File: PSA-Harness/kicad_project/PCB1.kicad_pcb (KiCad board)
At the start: 4 copper layers, 22.4 x 43.8 mm, 5 parts, among them J10 B2B_1, J11 B2B_2, J4 to_car_1, J5 to_car_2, J6 to_car_3

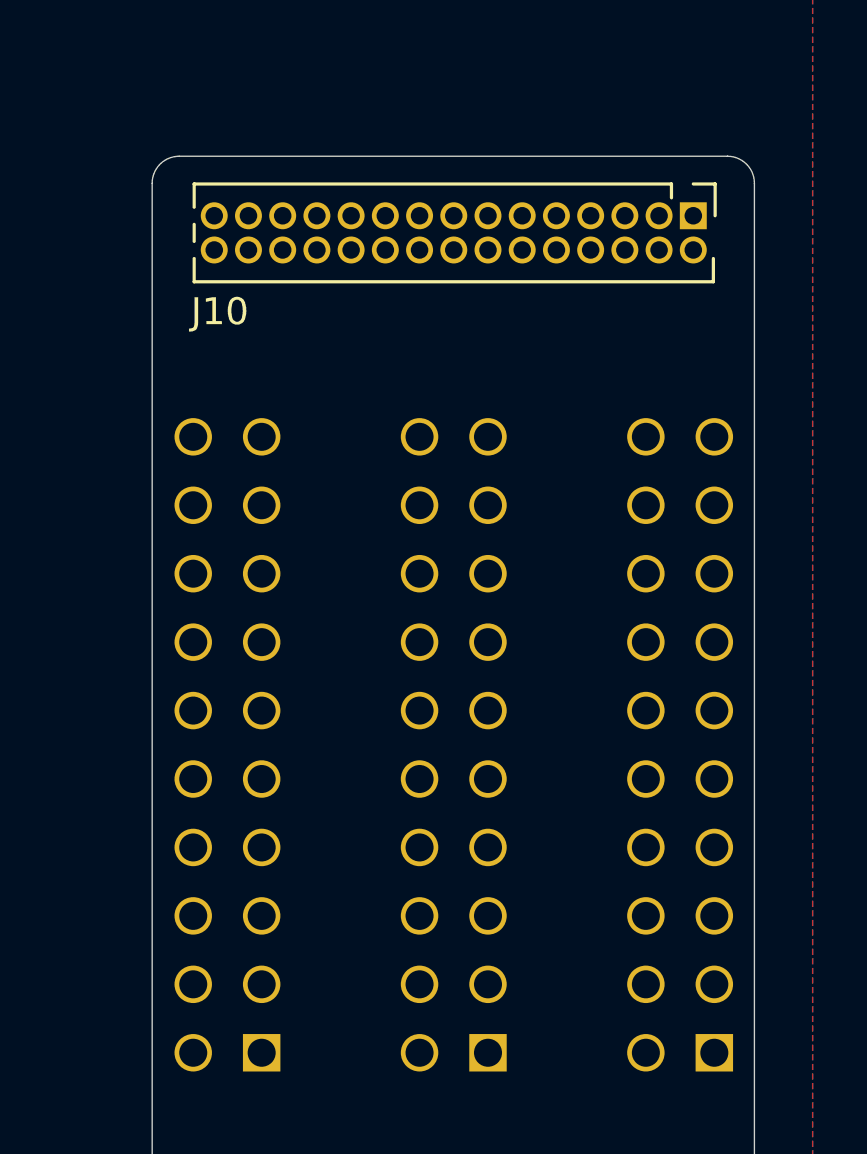
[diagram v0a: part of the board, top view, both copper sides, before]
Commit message: CAN routing PCB1
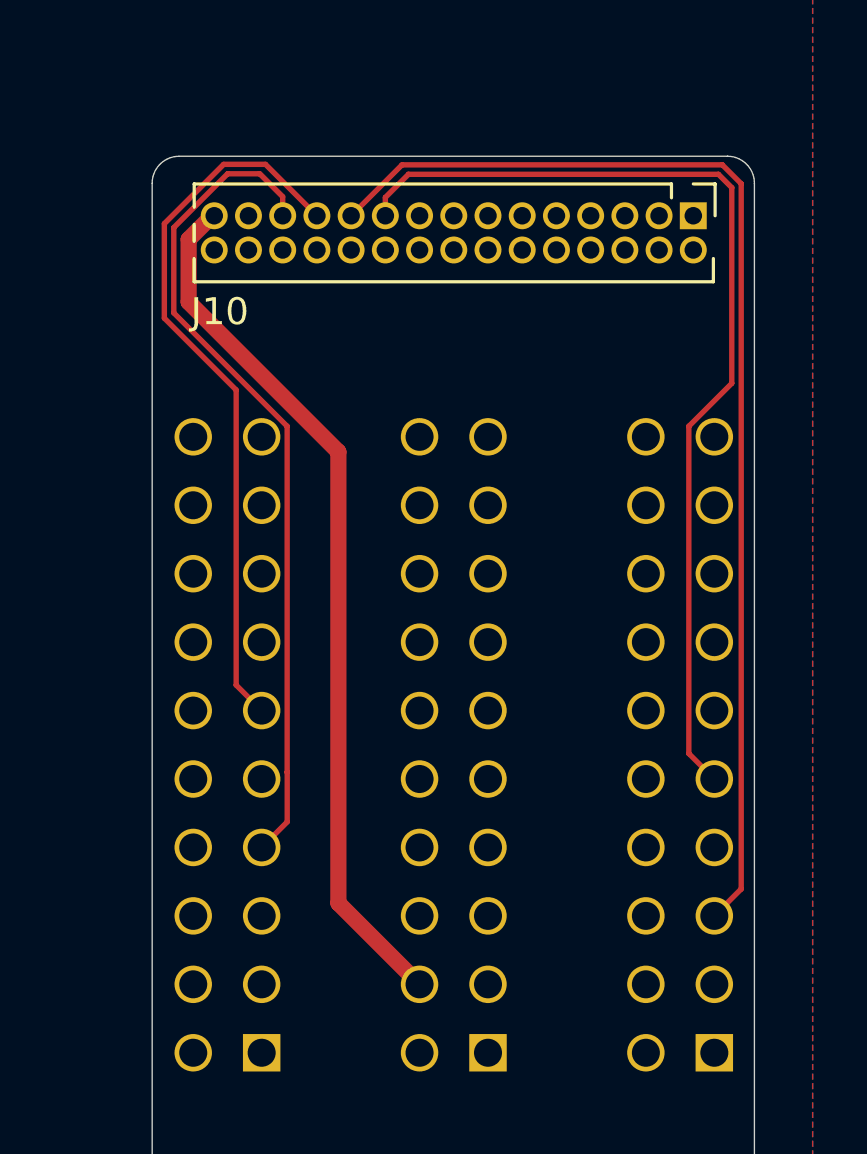
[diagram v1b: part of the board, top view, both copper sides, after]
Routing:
- net CAN2_L: track 0.00 -> 43.1 mm
- net CAN2_H: track 0.00 -> 37.1 mm
- net +12V: track 0.00 -> 32.5 mm
- net CAN1_L: track 0.00 -> 31.1 mm
- net CAN1_H: track 0.00 -> 26.9 mm

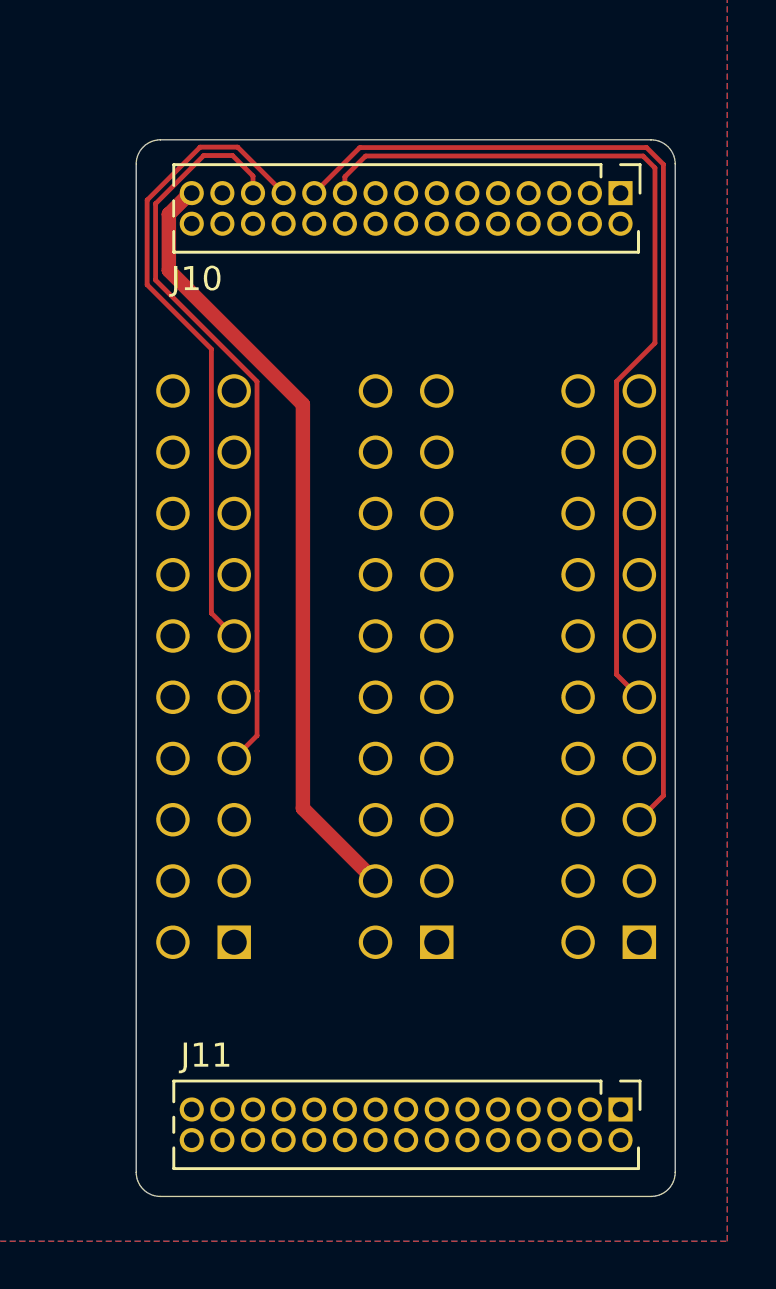
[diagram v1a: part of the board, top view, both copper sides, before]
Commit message: PCB1 routed
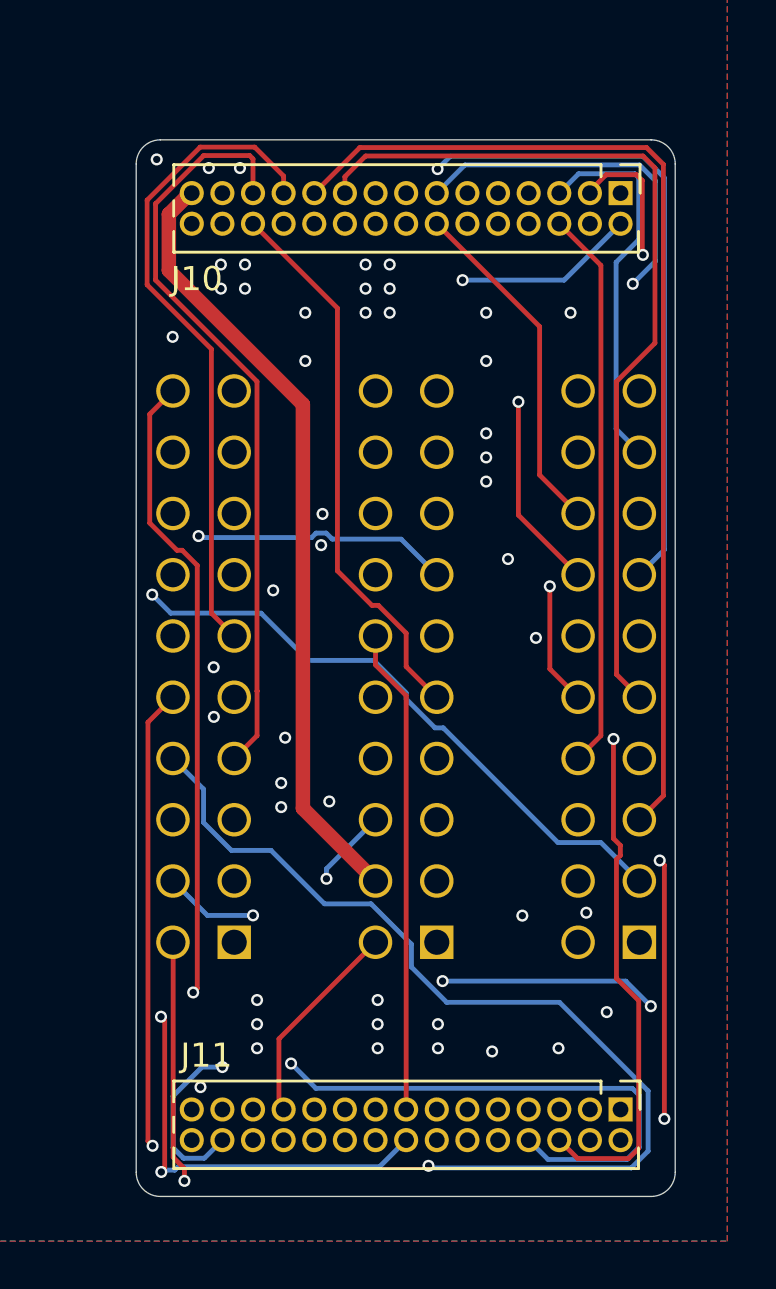
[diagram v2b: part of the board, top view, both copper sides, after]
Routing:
- net 1: track 0.00 -> 57.0 mm, vias 0 -> 2
- net 2: track 0.00 -> 54.8 mm, vias 0 -> 2
- net 50: track 0.00 -> 52.6 mm, vias 0 -> 3
- net 49: track 0.00 -> 48.6 mm, vias 0 -> 1
- net 48: track 0.00 -> 44.0 mm, vias 0 -> 1
- net 52: track 0.00 -> 42.1 mm, vias 0 -> 3
- net 54: track 0.00 -> 41.4 mm, vias 0 -> 1
- net 47: track 0.00 -> 41.1 mm, vias 0 -> 1
- net 28: track 0.00 -> 36.7 mm, vias 0 -> 1
- net 4: track 0.00 -> 34.9 mm, vias 0 -> 1
- net 30: track 0.00 -> 34.7 mm, vias 0 -> 1
- net 59: track 0.00 -> 34.5 mm, vias 0 -> 2
- net 12: track 0.00 -> 34.4 mm, vias 0 -> 1
- net 11: track 0.00 -> 33.4 mm
- net 29: track 0.00 -> 33.2 mm, vias 0 -> 1
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
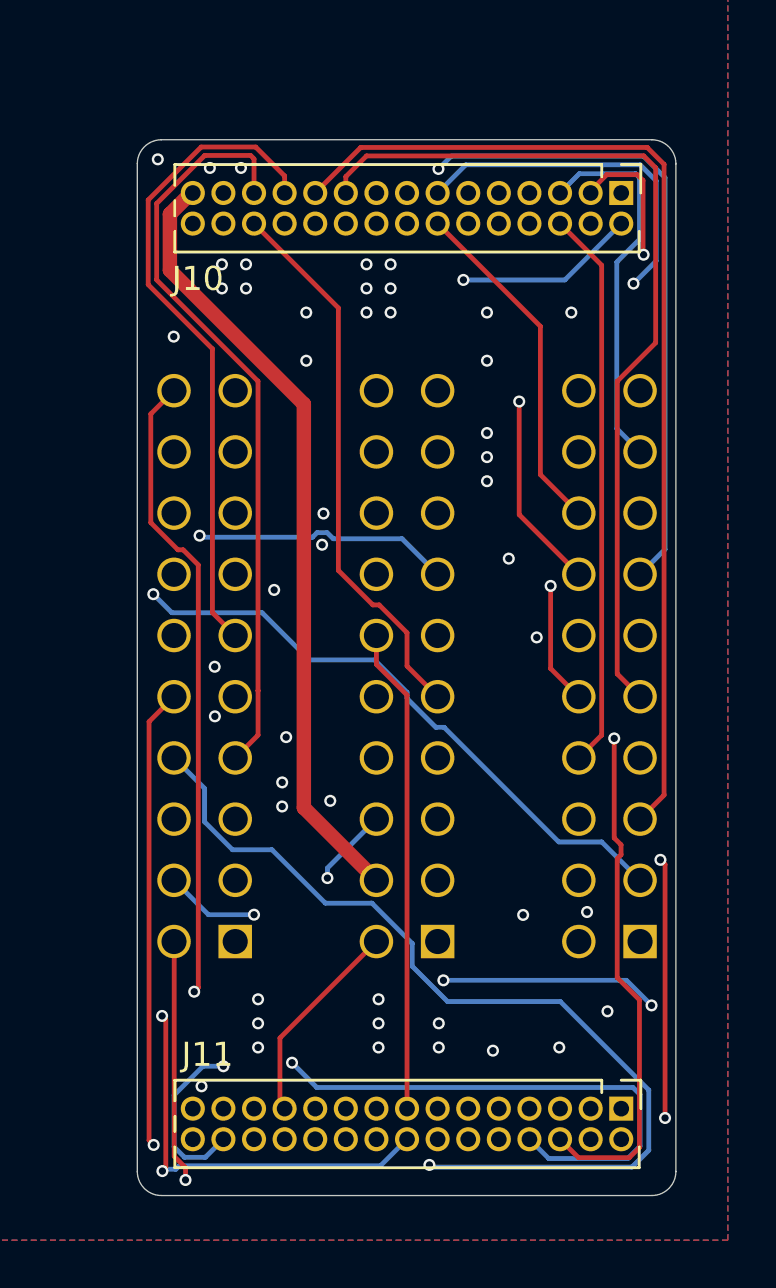
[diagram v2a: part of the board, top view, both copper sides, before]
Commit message: improve PCB1 clearences
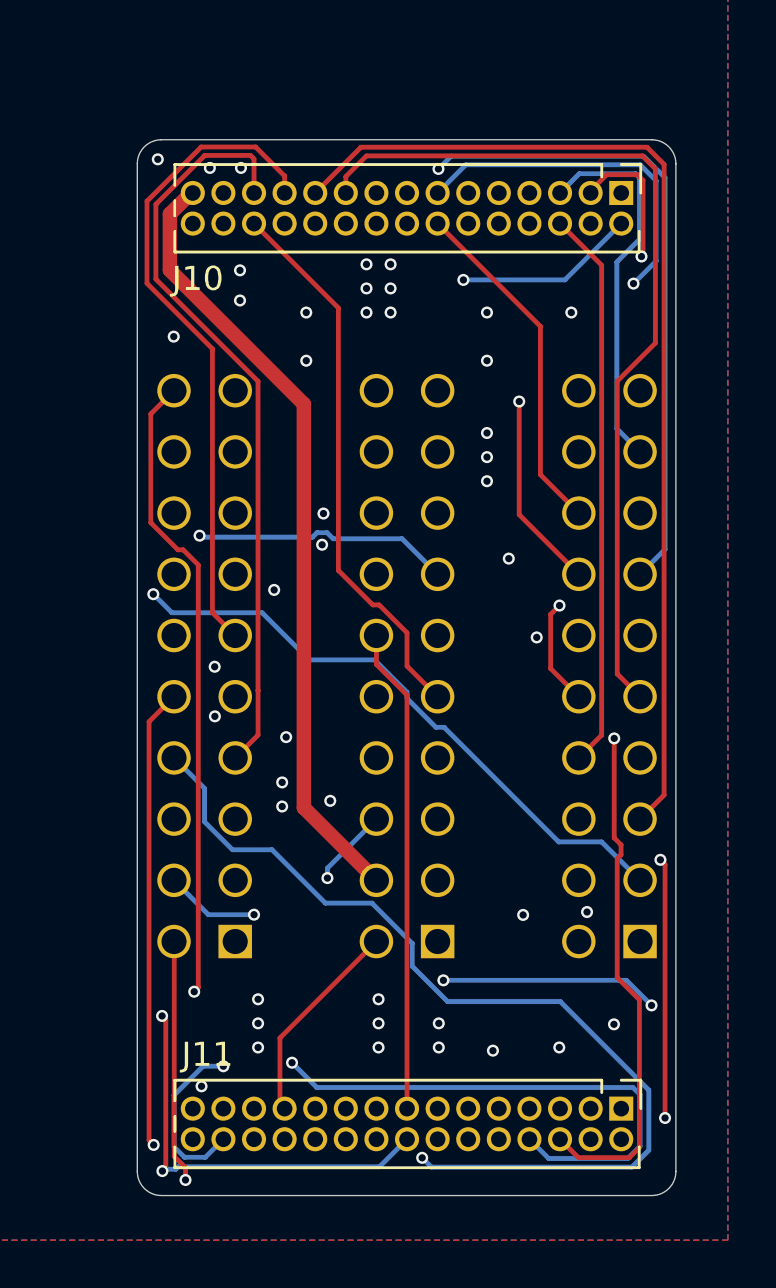
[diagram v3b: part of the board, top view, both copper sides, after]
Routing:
- net 16: track 18.5 -> 19.0 mm
- net GND: vias 34 -> 32
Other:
- rule pad_to_mask_clearance: 0.038 -> 0

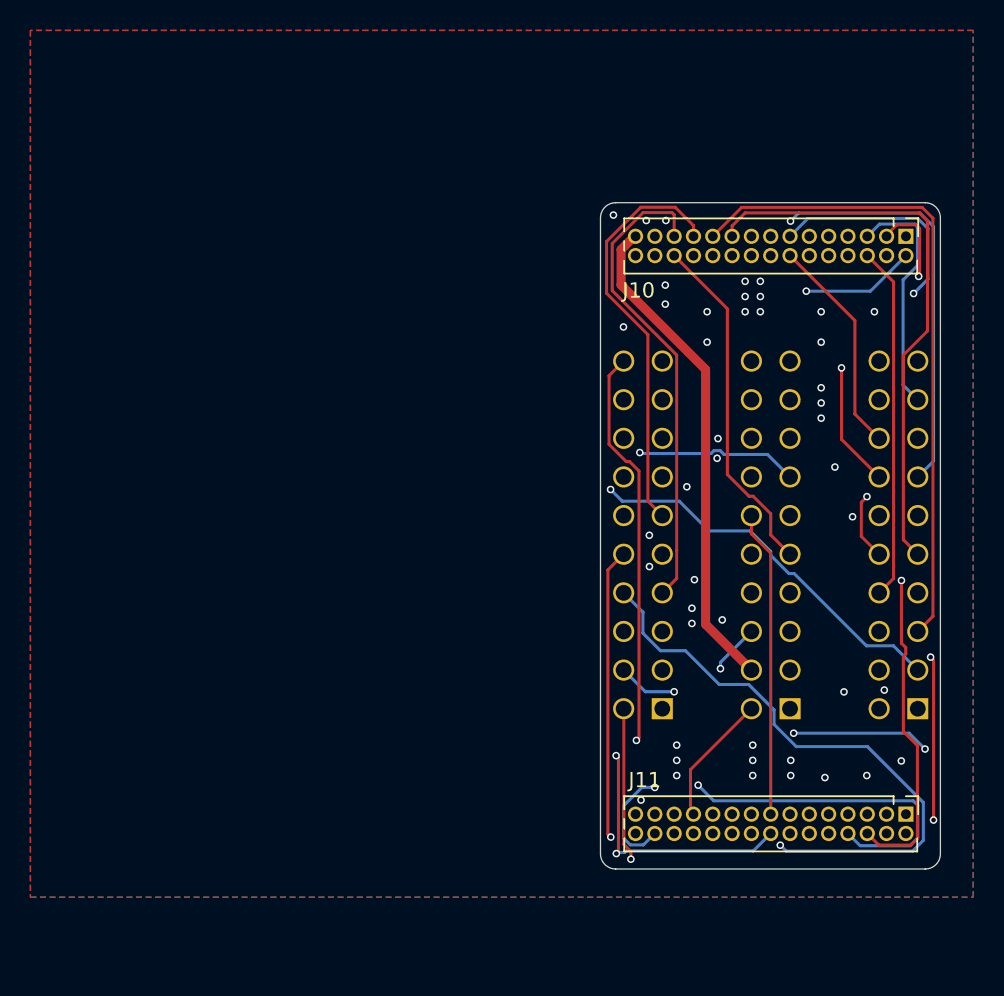
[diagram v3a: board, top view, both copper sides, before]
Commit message: chg: separate PCB1/2
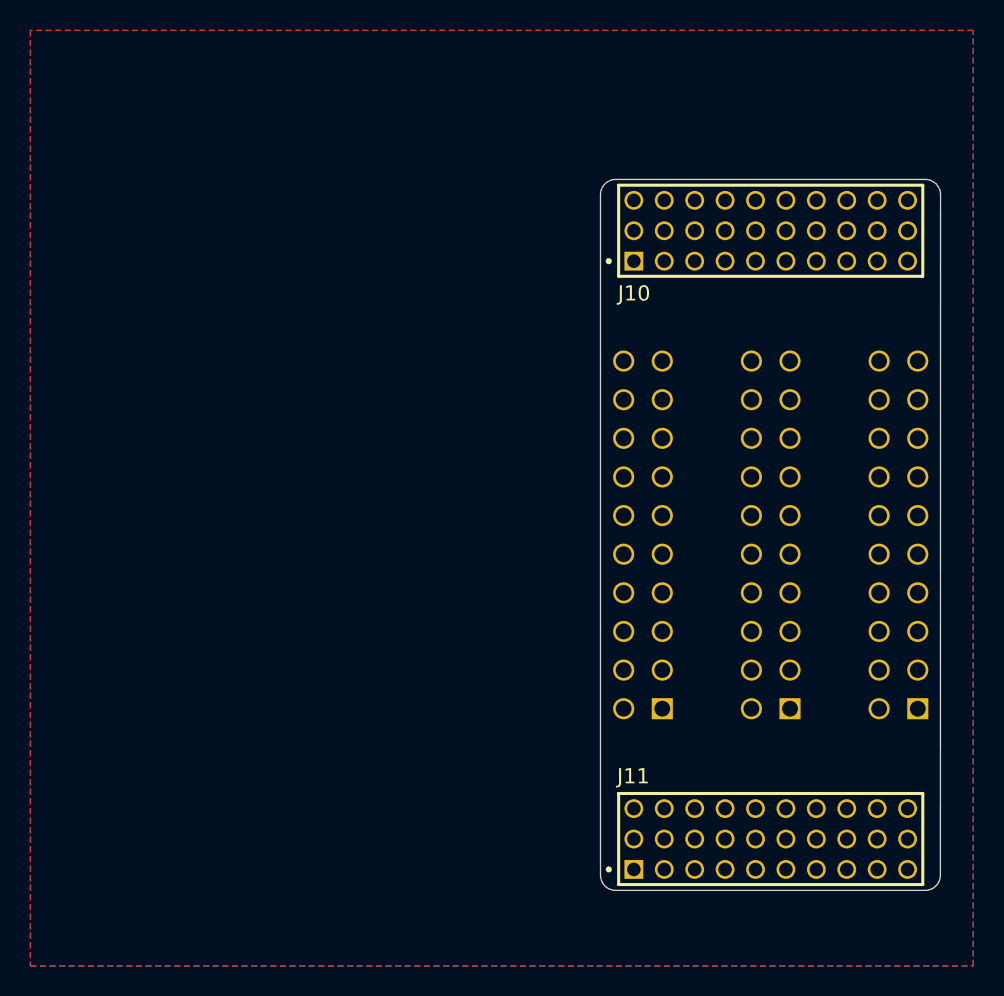
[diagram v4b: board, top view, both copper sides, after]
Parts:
- J10, J11: footprint Connector_PinHeader_1.27mm:PinHeader_2x15_P1.27mm_Vertical -> PSA:SAMTEC_TW-10-X-X-T-X-X
- moved J11 18.3 mm to (126.7, 144.2), turned to 0 degrees
- moved J10 18.0 mm to (126.7, 104.2), turned to 0 degrees
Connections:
- J10 pad 1: 11 -> GND
- J10 pad 11: 6 -> CAN2_H
- J10 pad 13: 4 -> 1
- J10 pad 17: 1 -> 4
- J10 pad 19: CAN2_H -> 6
- J10 pad 21: CAN2_L -> 7
- J10 pad 23: CAN1_H -> 8
- J10 pad 25: CAN1_L -> 9
- J10 pad 27: GND -> 10
- J10 pad 29: +12V -> 11
- J10 pad 3: 10 -> +12V
- J10 pad 5: 9 -> CAN1_L
- J10 pad 7: 8 -> CAN1_H
- J10 pad 9: 7 -> CAN2_L
- J11 pad 1: 43 -> 28
- J11 pad 11: 38 -> 34
- J11 pad 13: 37 -> 35
- J11 pad 17: 35 -> 37
- J11 pad 19: 34 -> 38
- J11 pad 21: 33 -> 39
- J11 pad 23: 31 -> 40
- J11 pad 25: 30 -> 41
- J11 pad 27: 29 -> 42
- J11 pad 29: 28 -> 43
- J11 pad 3: 42 -> 29
- J11 pad 5: 41 -> 30
- J11 pad 7: 40 -> 31
- J11 pad 9: 39 -> 33
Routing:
- net 1: track 57.0 -> 0.00 mm, vias 2 -> 0
- net 2: track 54.8 -> 0.00 mm, vias 2 -> 0
- net 50: track 52.6 -> 0.00 mm, vias 3 -> 0
- net 49: track 48.6 -> 0.00 mm, vias 1 -> 0
- net 48: track 44.0 -> 0.00 mm, vias 1 -> 0
- net CAN2_L: track 43.1 -> 0.00 mm
- net 52: track 42.1 -> 0.00 mm, vias 3 -> 0
- net 54: track 41.4 -> 0.00 mm, vias 1 -> 0
- net 47: track 41.1 -> 0.00 mm, vias 1 -> 0
- net CAN2_H: track 37.1 -> 0.00 mm
- net 28: track 36.7 -> 0.00 mm, vias 1 -> 0
- net 4: track 34.9 -> 0.00 mm, vias 1 -> 0
- net 30: track 34.7 -> 0.00 mm, vias 1 -> 0
- net 59: track 34.5 -> 0.00 mm, vias 2 -> 0
- net 12: track 34.4 -> 0.00 mm, vias 1 -> 0
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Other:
- board size 22.4 x 43.8 mm -> 22.4 x 46.8 mm
- rule pad_to_mask_clearance: 0 -> 0.038
